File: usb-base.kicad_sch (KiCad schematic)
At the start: 19 parts, among them J1 USB3_B, U1 CYUSB3082-FCAXI, U2 TPS25221, U3 TPS62161DSG, U4 LFE5U-25F-6BG256C, U6 TPS62162DSG

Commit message: Power supplies, oscillators, user IO breakout
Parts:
- added C10: 10u, Capacitor_SMD:C_0805_2012Metric, symbol Device:C_Small
- added C11: 22u, Capacitor_SMD:C_1206_3216Metric, symbol Device:C_Small
- added J2: USB_C_Receptacle, symbol Connector:USB_C_Receptacle
- added L3: 2.2u, Inductor_SMD:L_Sunlord_SWPA3015S, symbol Device:L_Small
- added R4: 20k, symbol Device:R_Small
- added R5: 7.5k, symbol Device:R_Small
- added U5: TPS62160DSG, Package_SON:WSON-8-1EP_2x2mm_P0.5mm_EP0.9x1.6mm_ThermalVias, symbol Regulator_Switching:TPS62160DSG
- added Y1: 24MHz, Crystal:Crystal_SMD_SeikoEpson_TSX3225-4Pin_3.2x2.5mm, symbol Oscillator:SG-5032CBN
- added Y2: 25MHz, Crystal:Crystal_SMD_SeikoEpson_TSX3225-4Pin_3.2x2.5mm, symbol Oscillator:SG-5032CBN
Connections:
- net +1V1: now also C11.1, L3.2, R5.1, U5.6 (VOS)
- net +1V8: no longer U1.C11 (VDDIO_QSPI), U1.M12 (VDDIO_XTAL)
- net +3.3V: now also Y1.1 (~{ST}), Y1.4 (VCC), Y2.1 (~{ST}), Y2.4 (VCC)
- net +3V3: now also U1.C11 (VDDIO_QSPI), U1.M12 (VDDIO_XTAL)
- net +5V: now also C10.1, U5.2 (VIN), U5.3 (EN)
- net GND: now also C10.2, C11.2, R4.2, U5.1 (PGND), U5.4 (AGND), U5.9 (PAD), Y1.2 (GND), Y2.2 (GND)
- net GPIO_1: now also U1.J12 (P9_7_I2S0-RXMCLK); no longer U1.J13 (P1_1_CC2)
- net P1CTL8: now also U4.P5 (PL68D/-/LLC_GPLL0C_IN/LDQ65); no longer U4.N4 (PL59A/+/HS/LDQ65)
- net P1CTL9: now also U4.T4 (PL65B/-/HS/LDQSN65); no longer U4.R5 (PL65A/+/HS/LDQS65)
- net P1D13: now also U4.N5 (PL65D/-/LDQ65); no longer U4.P5 (PL68D/-/LLC_GPLL0C_IN/LDQ65)
- net P1D5: now also U4.R5 (PL65A/+/HS/LDQS65); no longer U4.T4 (PL65B/-/HS/LDQSN65)
- net D1_5: now reaches U4.K12 (PR38B/-/HS/RDQ41)
- net D1_4: now reaches U4.K13 (PR38A/+/GR_PCLK3_0/HS/RDQ41)
- net D1_7: now reaches U4.L12 (PR38D/-/RDQ41)
- net D1_6: now reaches U4.L13 (PR38C/+/GR_PCLK3_1/RDQ41)
- net D1_10: now reaches U4.L14 (PR41C/+/RDQ41)
- net D1_1: now reaches U4.L15 (PR35B/-/PCLKC3_1/HS/RDQ41)
- net D1_0: now reaches U4.L16 (PR35A/+/PCLKT3_1/HS/RDQ41)
- net D1_25: now reaches U4.M12 (PR65C/+/RDQ65)
- net D1_14: now reaches U4.M13 (PR44C/+/RDQ41)
- net D1_11: now reaches U4.M14 (PR41D/-/RDQ41)
- net D1_3: now reaches U4.M15 (PR35D/-/PCLKC3_0/RDQ41)
- net D1_2: now reaches U4.M16 (PR35C/+/PCLKT3_0/RDQ41)
- net D1_26: now reaches U4.N12 (PR65D/-/RDQ65)
- net D1_16: now reaches U4.N13 (PR59A/+/HS/RDQ65)
- net D1_15: now reaches U4.N14 (PR44D/-/RDQ41)
- net D1_8: now reaches U4.N16 (PR41A/+/HS/RDQS41)
- net D1_27: now reaches U4.P12 (PR68D/-/LRC_GPLL0C_IN/RDQ65)
- net D1_20: now reaches U4.P13 (PR62A/+/HS/RDQ65)
- net D1_17: now reaches U4.P14 (PR59B/-/HS/RDQ65)
- net D1_9: now reaches U4.P15 (PR41B/-/HS/RDQSN41)
- net D1_12: now reaches U4.P16 (PR44A/+/HS/RDQ41)
- net D1_24: now reaches U4.R12 (PR65A/+/HS/RDQS65)
- net D1_22: now reaches U4.R13 (PR62C/+/RDQ65)
- net D1_21: now reaches U4.R14 (PR62B/-/HS/RDQ65)
- net D1_18: now reaches U4.R15 (PR59C/+/RDQ65)
- net D1_13: now reaches U4.R16 (PR44B/-/VREF1_3/HS/RDQ41)
- net D1_23: now reaches U4.T14 (PR62D/-/RDQ65)
- net D1_19: now reaches U4.T15 (PR59D/-/RDQ65)
- net D0_1: now reaches U4.B15 (PR11B/-/URC_GPLL0C_IN/HS/RDQ17)
- net D0_0: now reaches U4.B16 (PR11A/+/URC_GPLL0T_IN/HS/RDQ17)
- net D0_2: now reaches U4.C14 (PR11C/+/RDQ17)
- net D0_5: now reaches U4.C15 (PR14B/-/HS/RDQ17)
- net D0_4: now reaches U4.C16 (PR14A/+/HS/RDQ17)
- net D0_3: now reaches U4.D14 (PR11D/-/RDQ17)
- net D0_8: now reaches U4.D16 (PR17A/+/HS/RDQS17)
- net D0_6: now reaches U4.E14 (PR14C/+/RDQ17)
- net D0_9: now reaches U4.E15 (PR17B/-/HS/RDQSN17)
- net D0_13: now reaches U4.E16 (PR20D/-/RDQ17)
- net D0_10: now reaches U4.F13 (PR17C/+/RDQ17)
- net D0_7: now reaches U4.F14 (PR14D/-/RDQ17)
- net D0_12: now reaches U4.F15 (PR20C/+/RDQ17)
- net D0_14: now reaches U4.F16 (PR23A/+/HS/RDQ29)
- net D0_11: now reaches U4.G13 (PR20B/-/HS/RDQ17)
- net D0_16: now reaches U4.G14 (PR23C/+/VREF1_2/RDQ29)
- net D0_15: now reaches U4.G15 (PR23B/-/HS/RDQ29)
- net D0_20: now reaches U4.G16 (PR29A/+/GR_PCLK2_1/HS/RDQS29)
- net D0_18: now reaches U4.H13 (PR26B/-/HS/RDQ29)
- net D0_17: now reaches U4.H14 (PR23D/-/RDQ29)
- net D0_21: now reaches U4.H15 (PR29B/-/HS/RDQSN29)
- net D0_19: now reaches U4.J13 (PR26C/+/RDQ29)
- net D0_22: now reaches U4.J14 (PR29C/+/GR_PCLK2_0/RDQ29)
- net D0_25: now reaches U4.J15 (PR32B/-/PCLKC2_1/HS/RDQ29)
- net D0_24: now reaches U4.J16 (PR32A/+/PCLKT2_1/HS/RDQ29)
- net D0_23: now reaches U4.K14 (PR29D/-/RDQ29)
- net D0_27: now reaches U4.K15 (PR32D/-/PCLKC2_0/RDQ29)
- net D0_26: now reaches U4.K16 (PR32C/+/PCLKT2_0/RDQ29)
- net 25MHz: now reaches U4.A7 (PT38A/+/PCLKT0_0)
- net 25MHz: now also Y2.3 (OUT)
- net PMODE: now reaches U1.F11 (P13_0_PMODE)
- net 24MHz: now reaches U1.M13 (P5_1_XTALOUT)
- net 24MHz: now also Y1.3 (OUT)
- new net: R4.1, R5.2, U5.5 (FB)
- new net: L3.1, U5.7 (SW)
- new net: J2.A1 (GND), J2.A12 (GND), J2.B1 (GND), J2.B12 (GND)
- new net: J2.A4 (VBUS), J2.A9 (VBUS), J2.B4 (VBUS), J2.B9 (VBUS)
- no-connect marks 141 -> 86
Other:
- note added: "1.1V buck converter (FPGA core)"
- note added: "1.8V buck converter (USB 3)"
- note added: "2.5V linear regularor (FPGA VCCAUX)"
- note added: "3.3V buck converter (VCCIO)"
- note added: "SSPI MODE"
- note added: "USB inrush current limiting"
- moved on the sheet: C2, C5

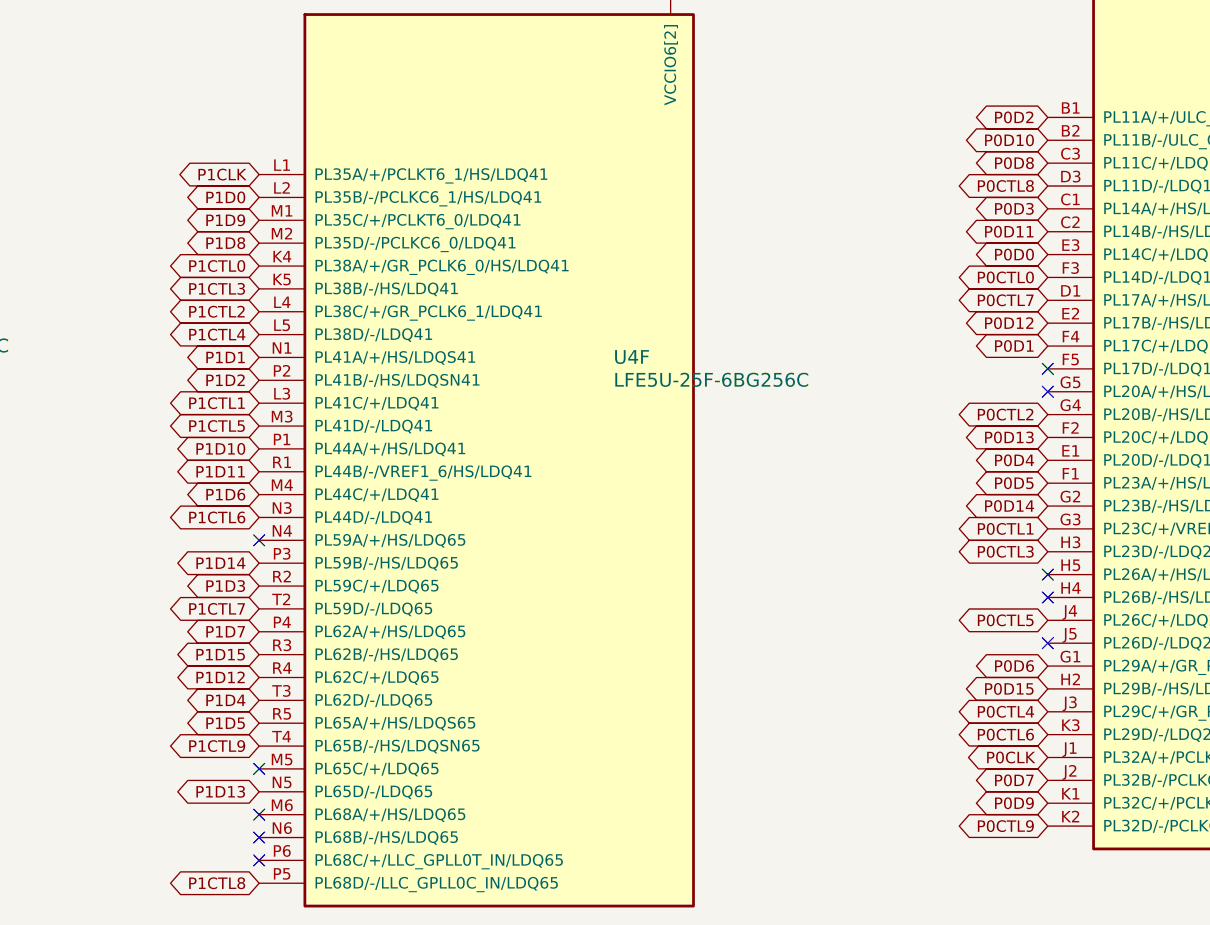
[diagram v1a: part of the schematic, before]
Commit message: Remove DDR support in favour of cleaner bus routing
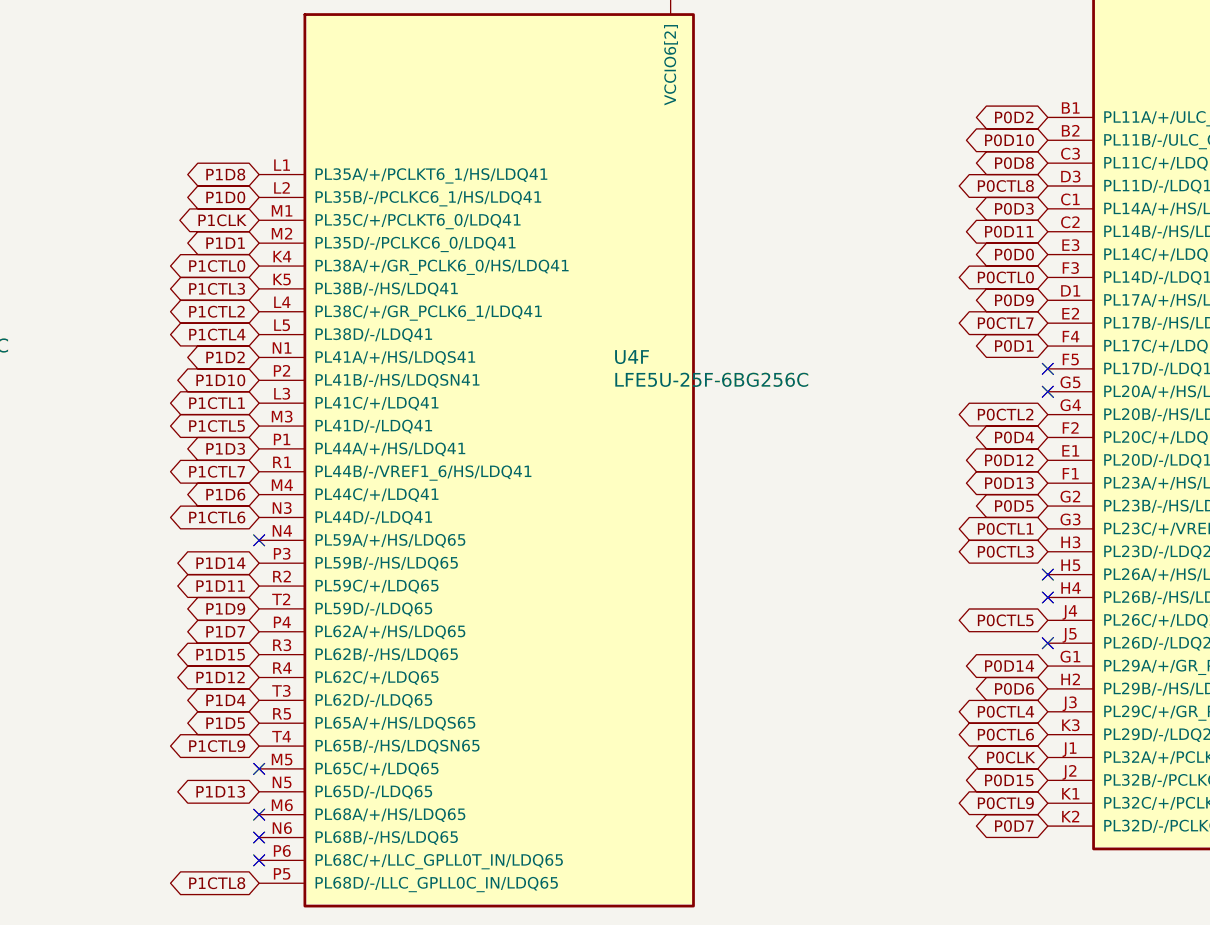
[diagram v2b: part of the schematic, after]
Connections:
- net P0CTL7: now also U4.E2 (PL17B/-/HS/LDQSN17); no longer U4.D1 (PL17A/+/HS/LDQS17)
- net P0CTL9: now also U4.K1 (PL32C/+/PCLKT7_0/LDQ29); no longer U4.K2 (PL32D/-/PCLKC7_0/LDQ29)
- net P0D12: now also U4.E1 (PL20D/-/LDQ17); no longer U4.E2 (PL17B/-/HS/LDQSN17)
- net P0D13: now also U4.F1 (PL23A/+/HS/LDQ29); no longer U4.F2 (PL20C/+/LDQ17)
- net P0D14: now also U4.G1 (PL29A/+/GR_PCLK7_1/HS/LDQS29); no longer U4.G2 (PL23B/-/HS/LDQ29)
- net P0D15: now also U4.J2 (PL32B/-/PCLKC7_1/HS/LDQ29); no longer U4.H2 (PL29B/-/HS/LDQSN29)
- net P0D4: now also U4.F2 (PL20C/+/LDQ17); no longer U4.E1 (PL20D/-/LDQ17)
- net P0D5: now also U4.G2 (PL23B/-/HS/LDQ29); no longer U4.F1 (PL23A/+/HS/LDQ29)
- net P0D6: now also U4.H2 (PL29B/-/HS/LDQSN29); no longer U4.G1 (PL29A/+/GR_PCLK7_1/HS/LDQS29)
- net P0D7: now also U4.K2 (PL32D/-/PCLKC7_0/LDQ29); no longer U4.J2 (PL32B/-/PCLKC7_1/HS/LDQ29)
- net P0D9: now also U4.D1 (PL17A/+/HS/LDQS17); no longer U4.K1 (PL32C/+/PCLKT7_0/LDQ29)
- net P1CLK: now also U4.M1 (PL35C/+/PCLKT6_0/LDQ41); no longer U4.L1 (PL35A/+/PCLKT6_1/HS/LDQ41)
- net P1CTL7: now also U4.R1 (PL44B/-/VREF1_6/HS/LDQ41); no longer U4.T2 (PL59D/-/LDQ65)
- net P1D1: now also U4.M2 (PL35D/-/PCLKC6_0/LDQ41); no longer U4.N1 (PL41A/+/HS/LDQS41)
- net P1D10: now also U4.P2 (PL41B/-/HS/LDQSN41); no longer U4.P1 (PL44A/+/HS/LDQ41)
- net P1D11: now also U4.R2 (PL59C/+/LDQ65); no longer U4.R1 (PL44B/-/VREF1_6/HS/LDQ41)
- net P1D2: now also U4.N1 (PL41A/+/HS/LDQS41); no longer U4.P2 (PL41B/-/HS/LDQSN41)
- net P1D3: now also U4.P1 (PL44A/+/HS/LDQ41); no longer U4.R2 (PL59C/+/LDQ65)
- net P1D8: now also U4.L1 (PL35A/+/PCLKT6_1/HS/LDQ41); no longer U4.M2 (PL35D/-/PCLKC6_0/LDQ41)
- net P1D9: now also U4.T2 (PL59D/-/LDQ65); no longer U4.M1 (PL35C/+/PCLKT6_0/LDQ41)
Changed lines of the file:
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@@
 	(global_label "P1D10"
 		(shape bidirectional)
-		(at 394.97 320.04 180)
+		(at 394.97 312.42 180)
 		(fields_autoplaced yes)
 		(effects
@@
 		)
 		(property "Intersheetrefs" "${INTERSHEET_REFS}"
-			(at 385.9145 320.04 0)
+			(at 384.705 312.42 0)
 			(hide yes)
 			(show_name no)
@@
 	(global_label "P0D13"
 		(shape bidirectional)
-		(at 482.6 318.77 180)
+		(at 482.6 323.85 180)
 		(fields_autoplaced yes)
 		(effects
@@
 		)
 		(property "Intersheetrefs" "${INTERSHEET_REFS}"
-			(at 472.335 318.77 0)
+			(at 473.5445 323.85 0)
 			(hide yes)
 			(show_name no)
@@
 	(global_label "P0D7"
 		(shape bidirectional)
-		(at 482.6 356.87 180)
+		(at 482.6 361.95 180)
 		(fields_autoplaced yes)
 		(effects
@@
 		)
 		(property "Intersheetrefs" "${INTERSHEET_REFS}"
-			(at 473.5445 356.87 0)
+			(at 472.4559 361.95 0)
 			(hide yes)
 			(show_name no)
@@
 	(global_label "P0D5"
 		(shape bidirectional)
-		(at 482.6 323.85 180)
+		(at 482.6 326.39 180)
 		(fields_autoplaced yes)
 		(effects
@@
 		)
 		(property "Intersheetrefs" "${INTERSHEET_REFS}"
-			(at 473.5445 323.85 0)
+			(at 473.5445 326.39 0)
 			(hide yes)
 			(show_name no)
@@
 	(global_label "P1D9"
 		(shape bidirectional)
-		(at 394.97 294.64 180)
+		(at 394.97 337.82 180)
 		(fields_autoplaced yes)
 		(effects
@@
 		)
 		(property "Intersheetrefs" "${INTERSHEET_REFS}"
-			(at 383.9188 294.64 0)
+			(at 385.9145 337.82 0)
 			(hide yes)
 			(show_name no)
@@
 	(global_label "P0D15"
 		(shape bidirectional)
-		(at 482.6 346.71 180)
+		(at 482.6 356.87 180)
 		(fields_autoplaced yes)
 		(effects
@@
 		)
 		(property "Intersheetrefs" "${INTERSHEET_REFS}"
-			(at 471.5488 346.71 0)
+			(at 473.5445 356.87 0)
 			(hide yes)
 			(show_name no)
@@
 	(global_label "P1D8"
 		(shape bidirectional)
-		(at 394.97 297.18 180)
+		(at 394.97 289.56 180)
 		(fields_autoplaced yes)
 		(effects
@@
 		)
 		(property "Intersheetrefs" "${INTERSHEET_REFS}"
-			(at 384.8259 297.18 0)
+			(at 385.9145 289.56 0)
 			(hide yes)
 			(show_name no)
@@
 	(global_label "P0D9"
 		(shape bidirectional)
-		(at 482.6 359.41 180)
+		(at 482.6 303.53 180)
 		(fields_autoplaced yes)
 		(effects
@@
 		)
 		(property "Intersheetrefs" "${INTERSHEET_REFS}"
-			(at 471.5488 359.41 0)
+			(at 473.5445 303.53 0)
 			(hide yes)
 			(show_name no)
@@
 	(global_label "P0D14"
 		(shape bidirectional)
-		(at 482.6 326.39 180)
+		(at 482.6 344.17 180)
 		(fields_autoplaced yes)
 		(effects
@@
 		)
 		(property "Intersheetrefs" "${INTERSHEET_REFS}"
-			(at 473.5445 326.39 0)
+			(at 471.5488 344.17 0)
 			(hide yes)
 			(show_name no)
@@
 	(global_label "P0D6"
 		(shape bidirectional)
-		(at 482.6 344.17 180)
+		(at 482.6 346.71 180)
 		(fields_autoplaced yes)
 		(effects
@@
 		)
 		(property "Intersheetrefs" "${INTERSHEET_REFS}"
-			(at 471.5488 344.17 0)
+			(at 471.5488 346.71 0)
 			(hide yes)
 			(show_name no)
@@
 	(global_label "P1CLK"
 		(shape bidirectional)
-		(at 394.97 289.56 180)
+		(at 394.97 294.64 180)
 		(fields_autoplaced yes)
 		(effects
@@
 		)
 		(property "Intersheetrefs" "${INTERSHEET_REFS}"
-			(at 385.9145 289.56 0)
+			(at 383.9188 294.64 0)
 			(hide yes)
 			(show_name no)
@@
 	(global_label "P1D3"
 		(shape bidirectional)
-		(at 394.97 335.28 180)
+		(at 394.97 320.04 180)
 		(fields_autoplaced yes)
 		(effects
@@
 		)
 		(property "Intersheetrefs" "${INTERSHEET_REFS}"
-			(at 384.705 335.28 0)
+			(at 385.9145 320.04 0)
 			(hide yes)
 			(show_name no)
@@
 	(global_label "P1D1"
 		(shape bidirectional)
-		(at 394.97 309.88 180)
+		(at 394.97 297.18 180)
 		(fields_autoplaced yes)
 		(effects
@@
 		)
 		(property "Intersheetrefs" "${INTERSHEET_REFS}"
-			(at 383.9188 309.88 0)
+			(at 384.8259 297.18 0)
 			(hide yes)
 			(show_name no)
@@
 	(global_label "P0D4"
 		(shape bidirectional)
-		(at 482.6 321.31 180)
+		(at 482.6 318.77 180)
 		(fields_autoplaced yes)
 		(effects
@@
 		)
 		(property "Intersheetrefs" "${INTERSHEET_REFS}"
-			(at 472.335 321.31 0)
+			(at 472.335 318.77 0)
 			(hide yes)
 			(show_name no)
@@
 	(global_label "P0D12"
 		(shape bidirectional)
-		(at 482.6 306.07 180)
+		(at 482.6 321.31 180)
 		(fields_autoplaced yes)
 		(effects
@@
 		)
 		(property "Intersheetrefs" "${INTERSHEET_REFS}"
-			(at 473.5445 306.07 0)
+			(at 472.335 321.31 0)
 			(hide yes)
 			(show_name no)
@@
 	(global_label "P0CTL7"
 		(shape bidirectional)
-		(at 482.6 303.53 180)
+		(at 482.6 306.07 180)
 		(fields_autoplaced yes)
 		(effects
@@
 		)
 		(property "Intersheetrefs" "${INTERSHEET_REFS}"
-			(at 473.5445 303.53 0)
+			(at 473.5445 306.07 0)
 			(hide yes)
 			(show_name no)
@@
 	(global_label "P1D11"
 		(shape bidirectional)
-		(at 394.97 322.58 180)
+		(at 394.97 335.28 180)
 		(fields_autoplaced yes)
 		(effects
@@
 		)
 		(property "Intersheetrefs" "${INTERSHEET_REFS}"
-			(at 385.9145 322.58 0)
+			(at 384.705 335.28 0)
 			(hide yes)
 			(show_name no)
@@
 	(global_label "P1CTL7"
 		(shape bidirectional)
-		(at 394.97 337.82 180)
+		(at 394.97 322.58 180)
 		(fields_autoplaced yes)
 		(effects
@@
 		)
 		(property "Intersheetrefs" "${INTERSHEET_REFS}"
-			(at 385.9145 337.82 0)
+			(at 385.9145 322.58 0)
 			(hide yes)
 			(show_name no)
@@
 	(global_label "P0CTL9"
 		(shape bidirectional)
-		(at 482.6 361.95 180)
+		(at 482.6 359.41 180)
 		(fields_autoplaced yes)
 		(effects
@@
 		)
 		(property "Intersheetrefs" "${INTERSHEET_REFS}"
-			(at 472.4559 361.95 0)
+			(at 471.5488 359.41 0)
 			(hide yes)
 			(show_name no)
@@
 	(global_label "P1D2"
 		(shape bidirectional)
-		(at 394.97 312.42 180)
+		(at 394.97 309.88 180)
 		(fields_autoplaced yes)
 		(effects
@@
 		)
 		(property "Intersheetrefs" "${INTERSHEET_REFS}"
-			(at 384.705 312.42 0)
+			(at 383.9188 309.88 0)
 			(hide yes)
 			(show_name no)
